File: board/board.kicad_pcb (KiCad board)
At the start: 2 copper layers, 50.8 x 22.9 mm, 18 parts, among them J1 MOTION DETECTOR, J2 EXT BUTTON, J3 GS2, J4 ~POWER, J5 GPWR, U3 ATTINY85-20PU

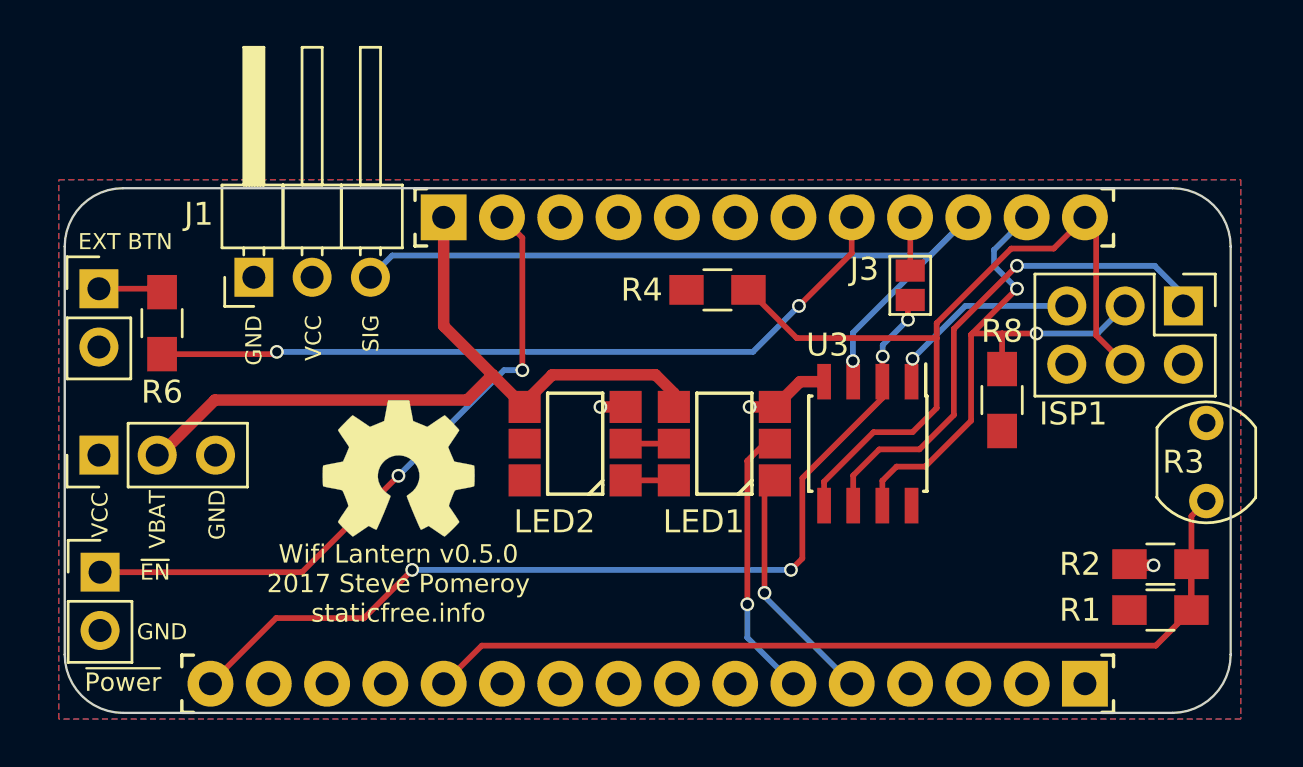
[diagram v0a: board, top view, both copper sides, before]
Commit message: Rework board to use Attiny84
MOAR GPIOS!

* Add battery level monitor
* Move RTC signal to power controller
* Add external wake signal breakout
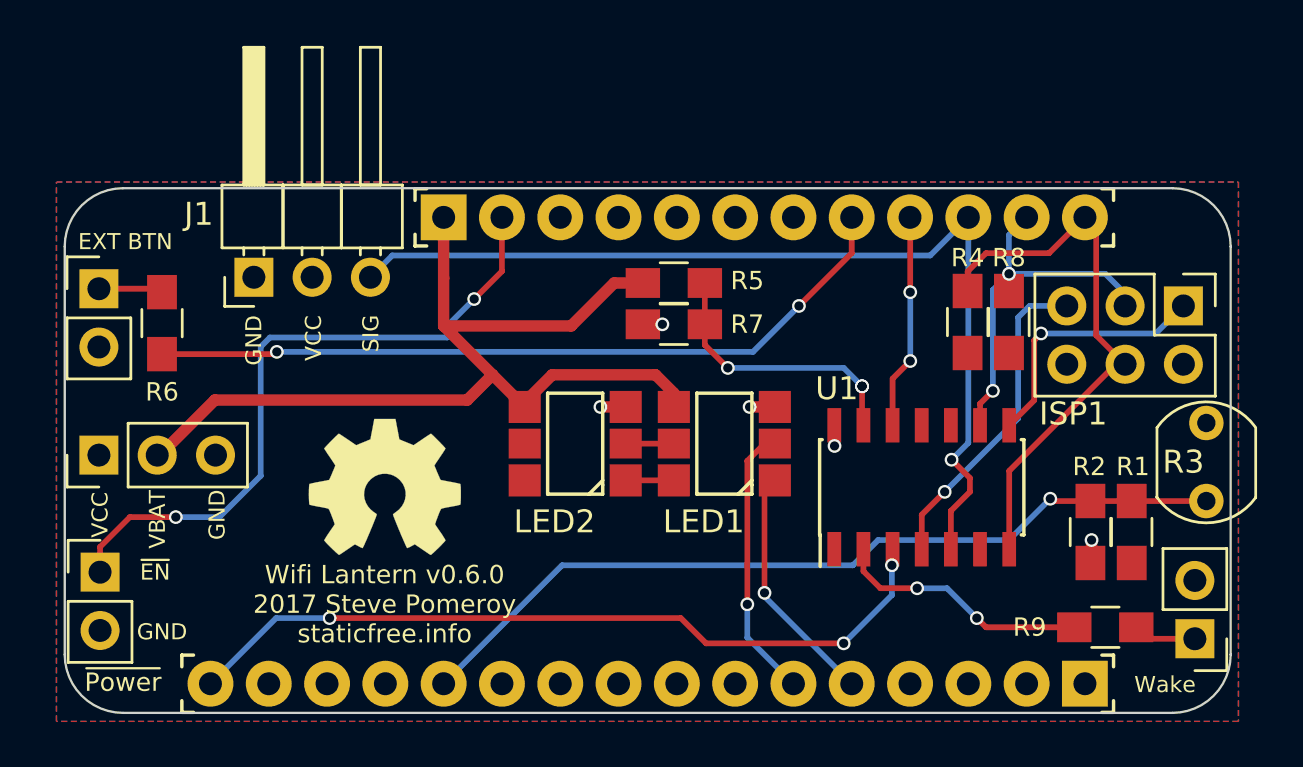
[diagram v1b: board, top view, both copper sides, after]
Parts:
- removed U3: ATTINY85-20PU, Housings_SOIC:SOIC-8_3.9x4.9mm_Pitch1.27mm
- added R5: 12K, Resistors_SMD:R_0805_HandSoldering, F.Cu at (138.3, 107.0)
- added R7: 30K, Resistors_SMD:R_0805_HandSoldering, F.Cu at (138.3, 108.8)
- added R9: 1K, Resistors_SMD:R_0805_HandSoldering, F.Cu at (157.1, 122.0)
- added U1: ATTINY84-20SSU, Housings_SOIC:SOIC-14_3.9x8.7mm_Pitch1.27mm, F.Cu at (149.1, 115.9)
- J3: value GS2 -> EXT WAKE; footprint Connectors:GS2 -> Pin_Headers:Pin_Header_Straight_1x02_Pitch2.54mm
- moved J3 19.8 mm to (161.0, 122.5), turned to 180 degrees
- moved R4 11.0 mm to (151.1, 108.7), turned to 90 degrees
- moved R1 3.62 mm to (158.2, 117.8), turned to 270 degrees
- moved R8 3.41 mm to (152.9, 108.7)
- moved R2 3.36 mm to (156.4, 117.8), turned to 270 degrees
- moved REF*** 1.00 mm to (125.7, 115.9)
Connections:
- net /SCL renamed /ATY_SCK
- net /SDA renamed /ATY_MOSI
- ISP1 pad 1: Net-(ISP1-Pad1) -> /ATY_MISO
- ISP1 pad 5: Net-(ISP1-Pad5) -> /~ATY_RST
- J3 pad 1: /D6 -> Net-(J3-Pad1)
- J3 pad 2: /~RESET -> GND
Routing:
- net Net-(ISP1-Pad1): track 22.7 -> 0.00 mm, vias 1 -> 0
- net /~ATY_RST: track 0.00 -> 14.2 mm, vias 0 -> 1
- net /BAT_MON: track 0.00 -> 12.5 mm, vias 0 -> 3
- net /ATY_MISO: track 0.00 -> 11.3 mm, vias 0 -> 1
- net /EXT_WAKE: track 0.00 -> 11.2 mm, vias 0 -> 2
- net /ATY_MOSI: track 35.5 -> 24.4 mm
- net /VBAT: track 34.1 -> 43.6 mm
- net /ATY_SCK: track 25.5 -> 16.6 mm
- net Net-(ISP1-Pad5): track 8.75 -> 0.00 mm, vias 1 -> 0
- net /~RESET: track 41.3 -> 34.2 mm, vias 4 -> 3
- net /D6: track 2.32 -> 9.38 mm, vias 0 -> 2
- net /D5: track 36.8 -> 43.0 mm
- net /A0: track 41.8 -> 38.0 mm, vias 0 -> 1
- net Net-(J3-Pad1): track 0.00 -> 2.76 mm
- net GND: track 6.01 -> 5.12 mm, vias 3 -> 5
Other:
- board text added: "(optional)"
- board text added: "Wake"
- board text added: "Wifi Lantern v0.6.0 2017 Steve Pomeroy staticfree.info"
- board text removed: "J3: short for ESP8266 built-in RTC reset"
- board text removed: "Wifi Lantern v0.5.0 2017 Steve Pomeroy staticfree.info"

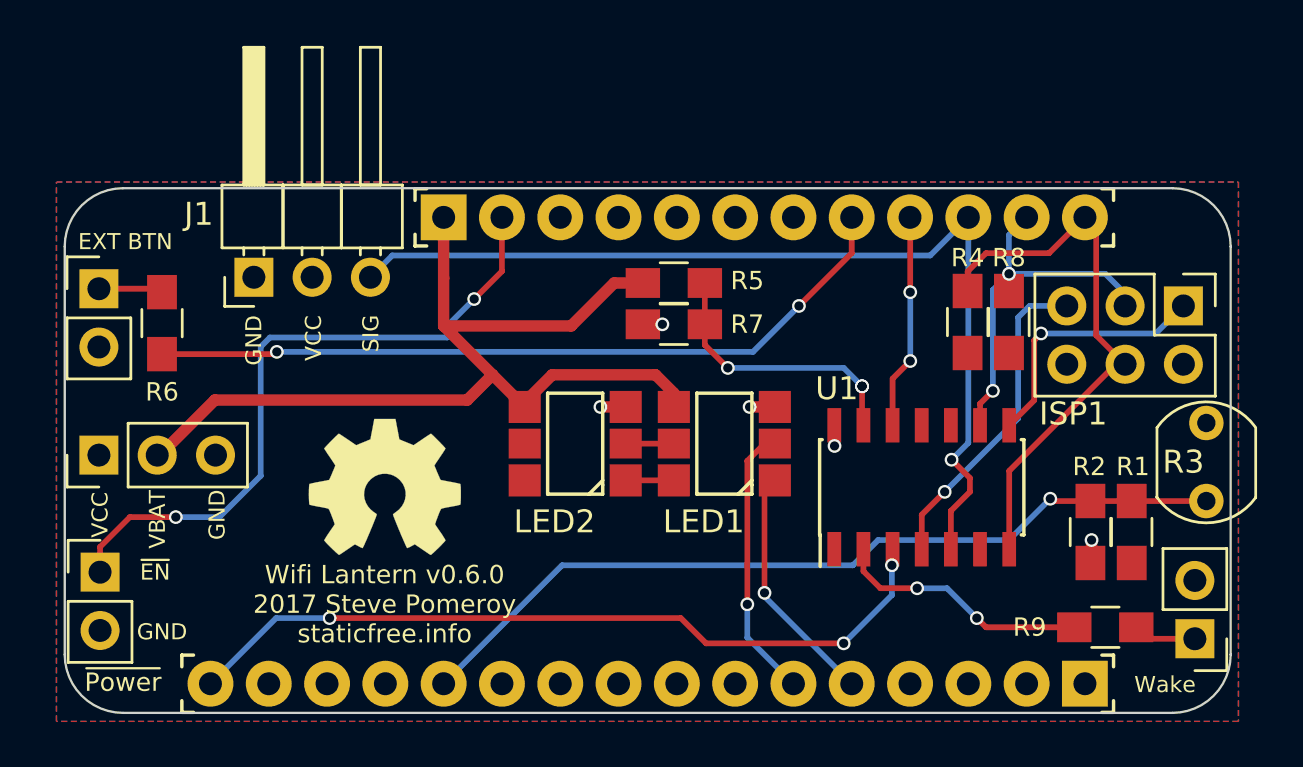
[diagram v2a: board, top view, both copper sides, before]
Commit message: Board revision 2
* Only connect motion detector to power manager
* Move ambient sensor to power manager
* Increase spacing on LEDs; move to hand solder footprint
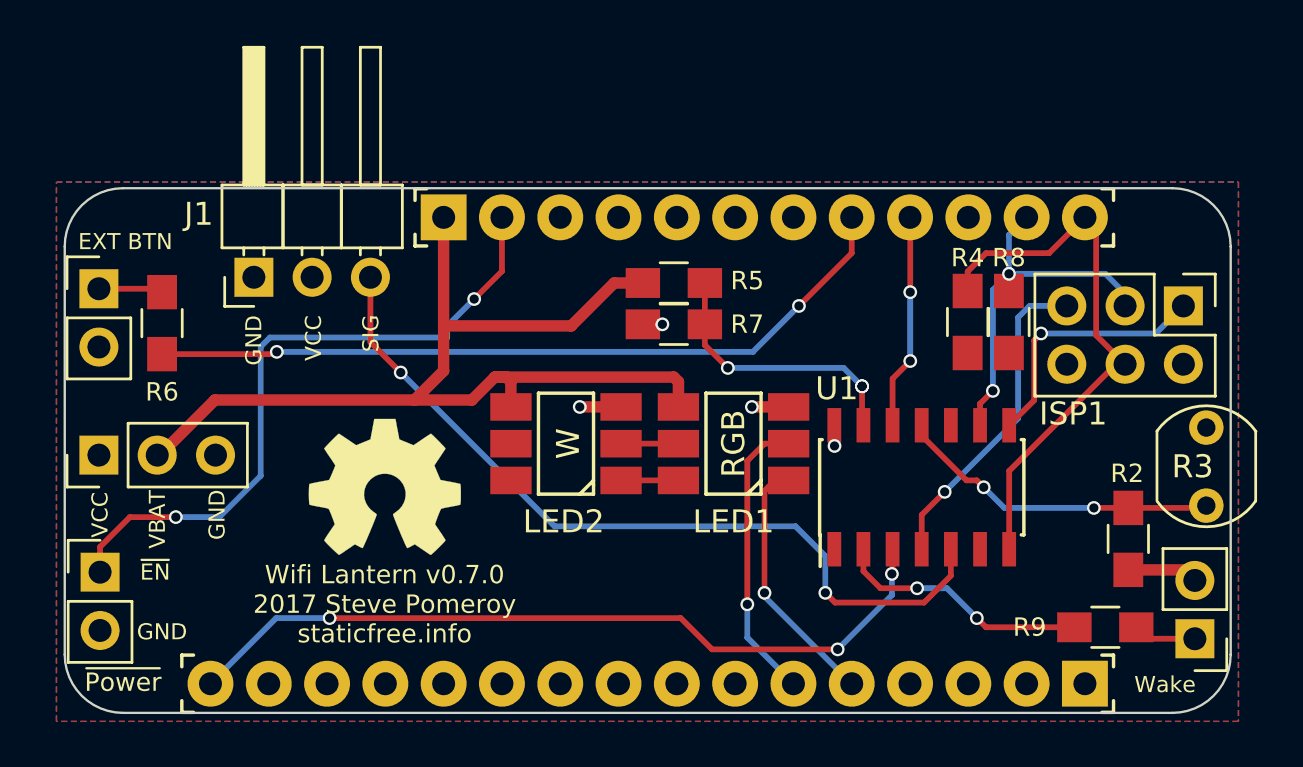
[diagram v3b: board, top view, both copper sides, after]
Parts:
- removed R1: 22.1K, Resistors_SMD:R_0805_HandSoldering
- LED1, LED2: footprint CrumpPrints:APA102 -> CrumpPrints:APA102_hand_solder
- U1: value ATTINY84-20SSU -> ATTINY841-SSU
- moved R3 3.20 mm to (161.5, 113.3), turned to 270 degrees
- moved R2 1.68 mm to (158.1, 118.2)
- moved LED1 0.40 mm to (140.9, 114.0)
- moved LED2 0.40 mm to (133.6, 114.0)
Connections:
- J1 pad 3: /D5 -> /MOTION_SIG
- JP1 pad 12: /A0 -> (no net)
- JP3 pad 10: /D5 -> (no net)
- R2 pad 1: /A0 -> /AMBIENT
- R3 pad 1: /A0 -> VCC
- R3 pad 2: GND -> /AMBIENT
- U1 pad 11: (no net) -> /AMBIENT
- U1 pad 5: /D5 -> /MOTION_SIG
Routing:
- net /D5: track 43.0 -> 0.00 mm, vias 1 -> 0
- net /A0: track 38.0 -> 0.00 mm, vias 1 -> 0
- net /MOTION_SIG: track 0.00 -> 36.2 mm, vias 0 -> 2
- net /AMBIENT: track 0.00 -> 14.3 mm, vias 0 -> 2
- net GND: track 5.12 -> 8.39 mm, vias 5 -> 4
- net /VBAT: track 43.6 -> 45.5 mm
- net (no net): track 0.00 -> 0.85 mm
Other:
- board text added: "RGB"
- board text added: "W"
- board text added: "Wifi Lantern v0.7.0 2017 Steve Pomeroy staticfree.info"
- board text removed: "Wifi Lantern v0.6.0 2017 Steve Pomeroy staticfree.info"
